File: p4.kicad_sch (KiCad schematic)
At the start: 45 parts, among them U1 W25Q128JVS, U3 TLV62569DBV, Y1 40MHz(+-10 ppm) C501798

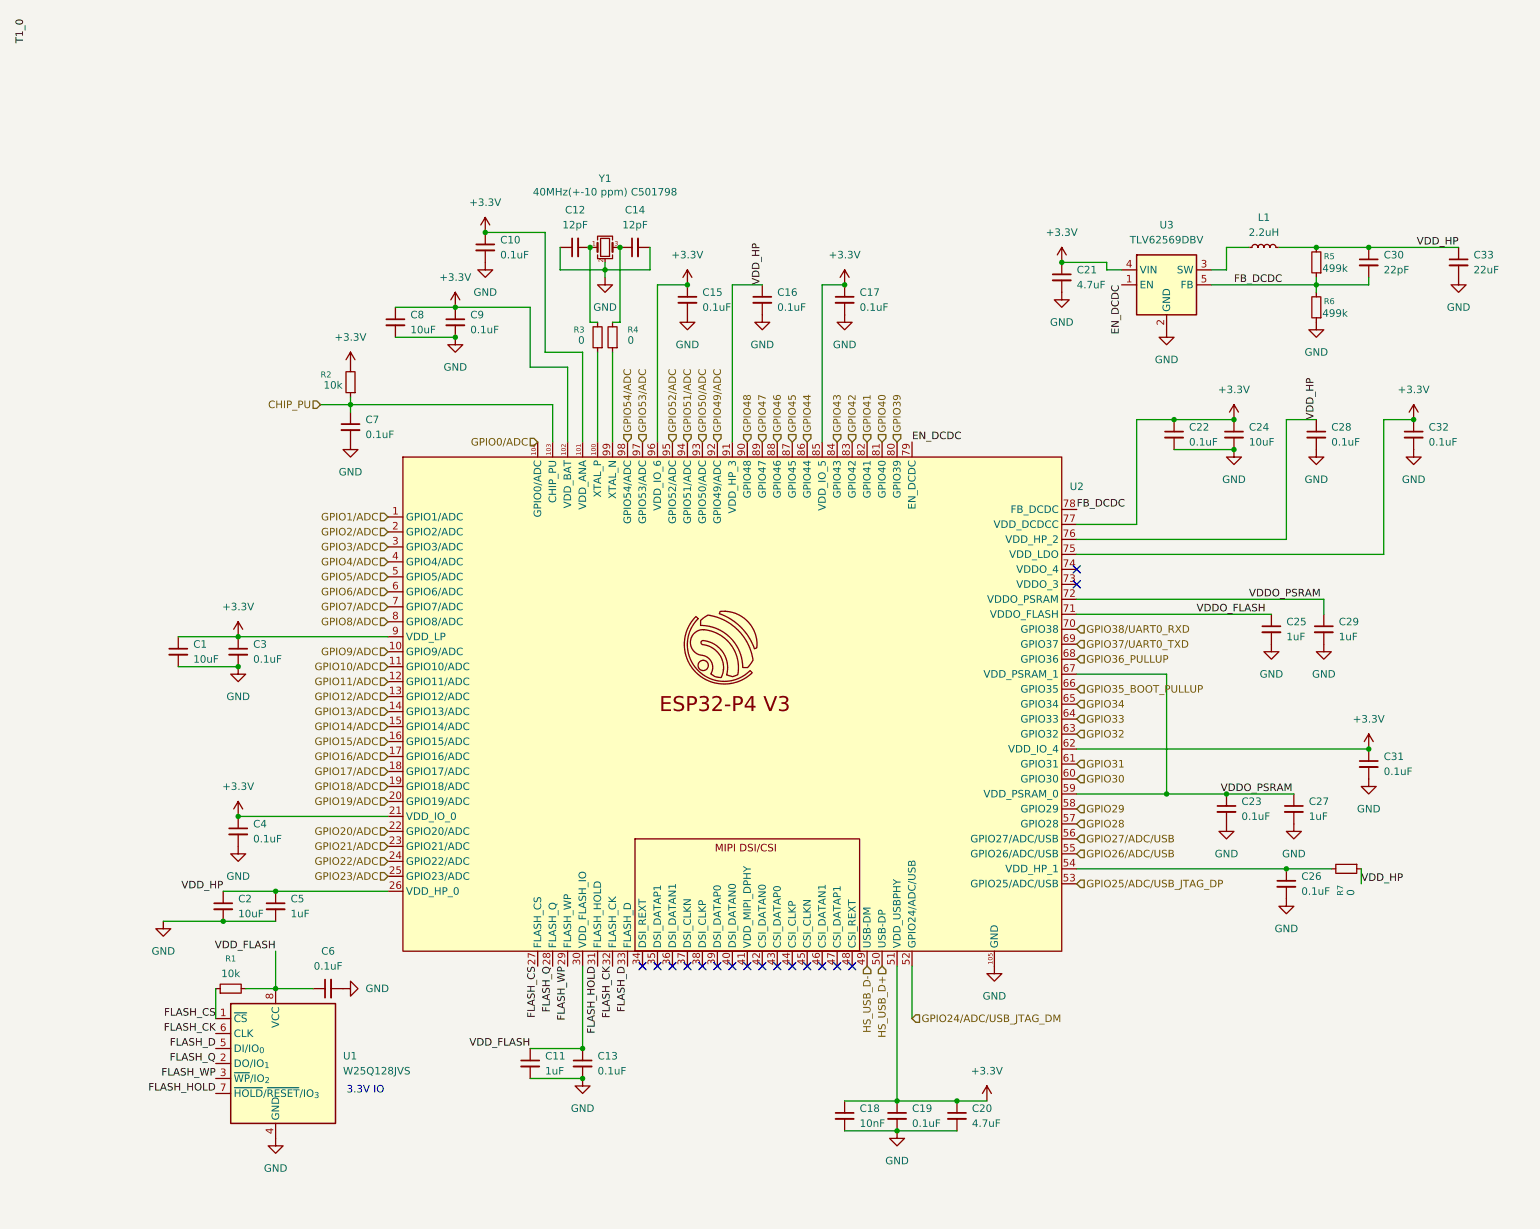
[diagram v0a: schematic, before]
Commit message: More schematic work. Mostly on Ethernet
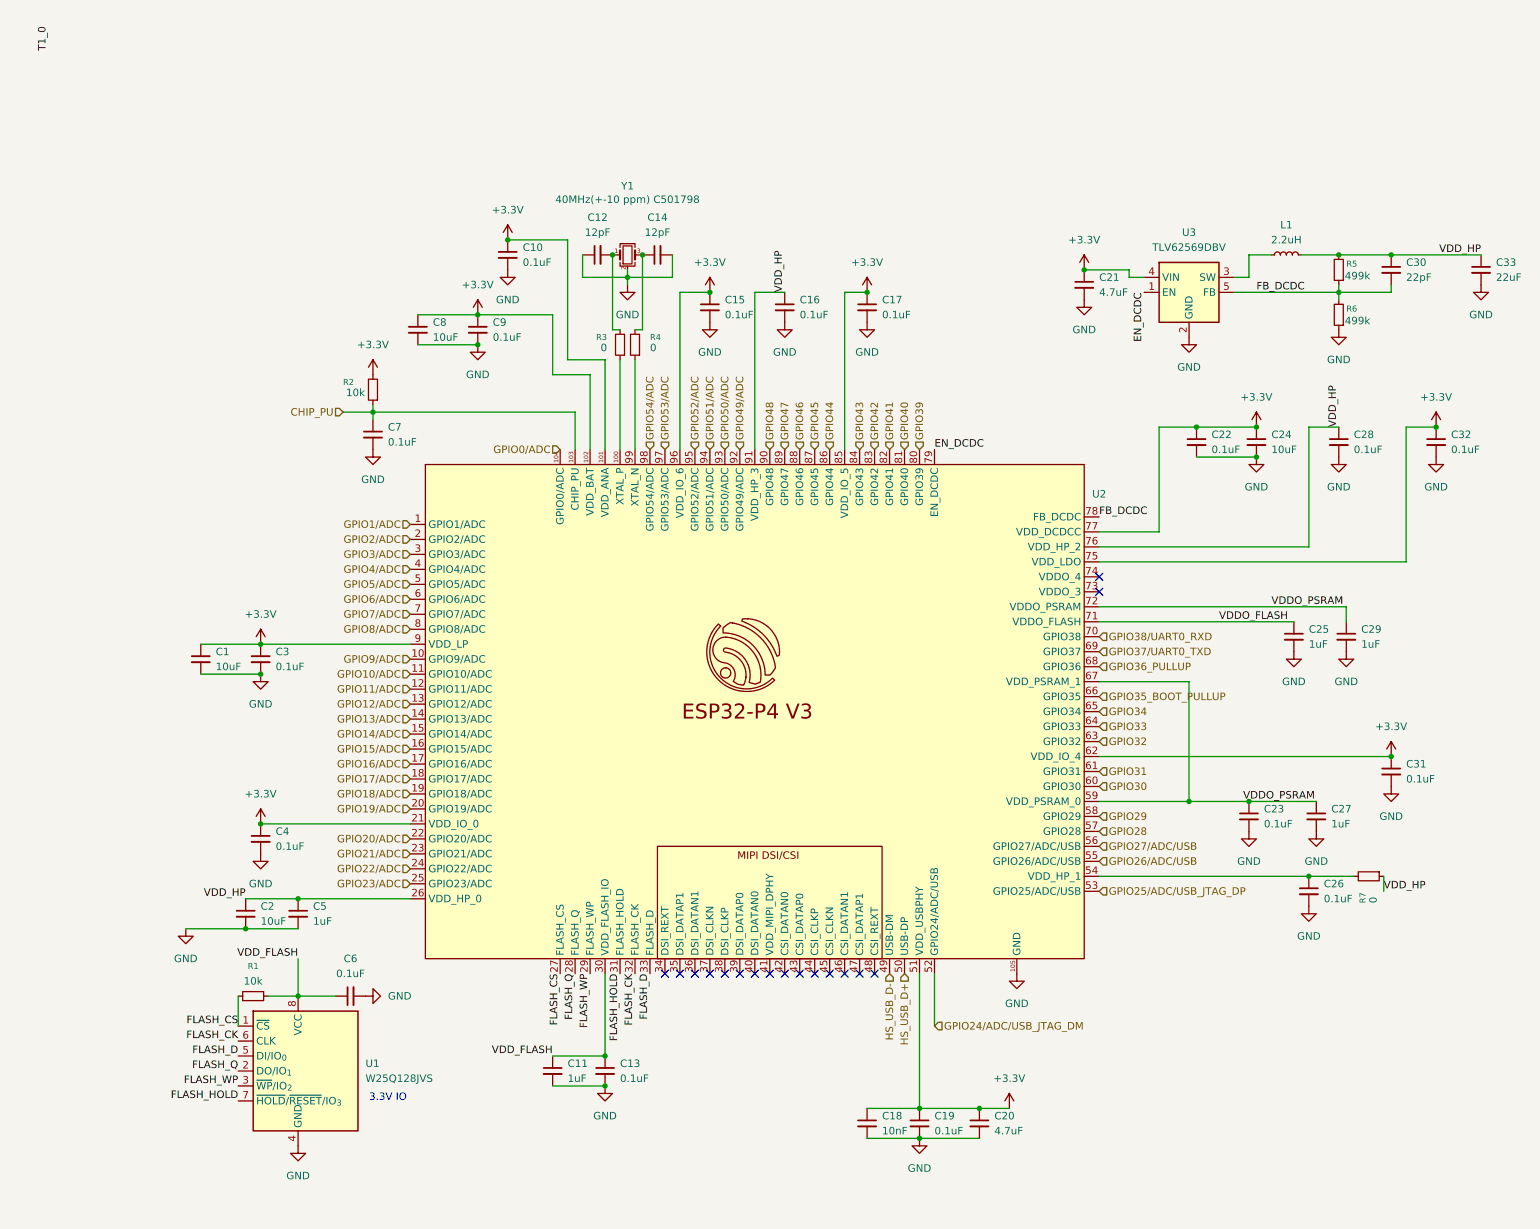
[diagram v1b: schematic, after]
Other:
- moved on the sheet: C1, C10, C11, C12, C13, C14, C15, C16, C17, C18, C19, C2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

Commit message: More USB schematic work
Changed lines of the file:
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@@
+		)
+	)
+	(label "SCL"
+		(at 200.2157 198.2788 270)
+		(effects
+			(font
+				(size 1.27 1.27)
+			)
+			(justify right bottom)
 		)
 	)

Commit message: Polish for v1
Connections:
- net VDDO_FLASH is gone; now on net VDD_FLASH: C25.1, U2.71 (VDDO_FLASH)
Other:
- moved on the sheet: C1, C10, C11, C12, C13, C14, C15, C16, C17, C18, C19, C2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
